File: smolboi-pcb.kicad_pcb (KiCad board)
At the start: 2 copper layers, 228.6 x 88.9 mm, 114 parts, among them SW1 ESC, SW10 O, SW11 P, SW12 Bksp, SW13 Tab, SW14 A, SW15 S, SW16 D, SW17 F, SW18 G, SW19 H, SW2 Q, SW20 J, SW21 K, SW22 L, SW23 ;, SW24 ', SW25 Shift, SW26 Z, SW27 X, SW28 C, SW29 V, SW3 W, SW30 B, SW31 N, SW32 M, SW33 ,, SW34 ., SW35 /, SW36 CpsLk, SW37 Ctrl, SW38 Win, SW39 Alt, SW4 E, SW40 FUP, SW41 FDN, SW42 Space, SW43 FRI, SW44 Left, SW45 Del, SW46 Enter, SW47 SW_Push, SW48 SW_Push, SW5 R, SW6 T, SW7 Y, SW8 U, SW9 I, U1 STM32F103C8Tx, U2 PRTR5V0U2X, U3 XC6206, Y1 8MHz

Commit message: staggered layout, routed diff pair on right side
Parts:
- SW1, SW10, SW11, SW14, SW15, SW16, SW17, SW18, SW19, SW2, SW20, SW21, SW22, SW23, SW26, SW27, SW28, SW29, SW3, SW30, SW31, SW32, SW33, SW34, SW35, SW36, SW4, SW40, SW41, SW43, SW44, SW45, SW46, SW5, SW6, SW7, SW8, SW9: footprint MX_Only:MXOnly-1U-Hotswap -> MX_Only:MXOnly-1U-NoLED
- SW12, SW25: footprint MX_Only:MXOnly-1U-Hotswap -> MX_Only:MXOnly-1.75U-NoLED
- SW13, SW37, SW38, SW39: footprint MX_Only:MXOnly-1U-Hotswap -> MX_Only:MXOnly-1.25U-NoLED
- SW24: footprint MX_Only:MXOnly-1U-Hotswap -> MX_Only:MXOnly-1.5U-NoLED
- SW42: footprint MX_Only:MXOnly-3U-Hotswap -> MX_Only:MXOnly-2U-NoLED
- moved SW48 80.4 mm to (350.3, 119.0), turned to 0 degrees
- moved C8 77.0 mm to (356.6, 57.1)
- moved C9 77.0 mm to (352.7, 55.4)
- moved U3 77.0 mm to (355.1, 55.4)
- moved R3 76.2 mm to (351.0, 45.5)
- moved U2 76.2 mm to (349.2, 50.8)
- moved USB1 76.2 mm to (349.2, 34.5)
- moved R4 76.0 mm to (347.5, 45.5)
- moved F1 74.4 mm to (342.6, 55.9)
- moved R5 72.2 mm to (345.3, 119.0), turned to 90 degrees
- moved C5 67.3 mm to (339.2, 109.1)
- moved U1 67.3 mm to (334.8, 104.6)
- moved C2 67.3 mm to (338.8, 99.6)
- moved C3 67.3 mm to (329.9, 100.7)
- moved C4 67.3 mm to (333.7, 111.0)
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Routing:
- net col2: track 60.9 -> 0.00 mm
- net col6: track 60.9 -> 0.00 mm
- net col1: track 60.8 -> 0.00 mm
- net col0: track 60.8 -> 0.00 mm
- net col10: track 60.7 -> 0.00 mm
- net col4: track 60.6 -> 0.00 mm
- net col11: track 60.4 -> 0.00 mm
- net col3: track 60.4 -> 0.00 mm
- net col8: track 60.3 -> 0.00 mm
- net col9: track 59.7 -> 0.00 mm
- net col5: track 44.1 -> 0.00 mm
- net col7: track 40.2 -> 0.00 mm
- net BOOT0: track 0.00 -> 9.03 mm
- net Net-(R4-Pad1): track 0.00 -> 2.96 mm
- net Net-(R3-Pad1): track 0.00 -> 2.72 mm
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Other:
- board size 228.6 x 88.9 mm -> 242.9 x 87.6 mm

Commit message: gnd fill around oscillator, all pwr routed, NRST vias
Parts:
- moved C9 18.7 mm to (335.0, 61.5), turned to 180 degrees
- moved U3 17.9 mm to (338.2, 61.4)
- moved C8 15.6 mm to (341.6, 61.4)
- moved D42 13.5 mm to (283.8, 110.5), turned to 90 degrees
- moved D44 8.90 mm to (359.4, 111.1), turned to 180 degrees
- moved D10 6.29 mm to (336.6, 53.3)
- moved D12 5.82 mm to (382.3, 53.3)
- moved D15 5.68 mm to (208.3, 72.4)
- moved D16 5.68 mm to (227.3, 72.4)
- moved D41 5.68 mm to (255.9, 110.5)
- moved D14 5.68 mm to (189.2, 72.4)
- moved D17 5.68 mm to (246.4, 72.4)
- moved D20 5.68 mm to (303.5, 72.4)
- moved D21 5.68 mm to (322.6, 72.4)
- moved D22 5.68 mm to (341.6, 72.4)
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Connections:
- SW43 pad 2: col8 -> col7
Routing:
- net row2: track 0.00 -> 209.1 mm
- net row1: track 0.00 -> 205.4 mm
- net row0: track 0.00 -> 202.1 mm
- net row3: track 0.00 -> 176.6 mm
- net +3V3: track 0.00 -> 129.2 mm, vias 0 -> 7
- net GND: track 0.00 -> 119.1 mm, vias 0 -> 5
- net col6: track 0.00 -> 67.3 mm
- net col1: track 0.00 -> 66.3 mm
- net col9: track 0.00 -> 65.9 mm
- net col2: track 0.00 -> 64.3 mm
- net col10: track 0.00 -> 63.3 mm
- net col4: track 0.00 -> 63.3 mm
- net col3: track 0.00 -> 63.3 mm
- net col7: track 0.00 -> 63.3 mm
- net col0: track 0.00 -> 62.5 mm
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- added copper zone on B.Cu, net GND
- added copper zone on F.Cu, net GND
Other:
- outline, holes or cut-outs redrawn
- net class Power: trace_width 0.381 -> 0.3

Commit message: routed matrix
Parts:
- removed SW47: SW_Push, Button_Switch_SMD:SW_SPST_SKQG_WithStem
- moved C1 8.29 mm to (330.2, 112.6), turned to 180 degrees
- moved R5 6.05 mm to (342.7, 113.5)
- moved SW48 6.05 mm to (347.7, 113.5)
- moved C4 1.01 mm to (330.2, 111.4)
- moved C9 0.30 mm to (335.3, 61.4), turned to 270 degrees
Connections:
- U1 pad 14: Net-(U1-Pad14) -> col0
- U1 pad 15: Net-(U1-Pad15) -> col1
- U1 pad 16: Net-(U1-Pad16) -> col2
- U1 pad 17: Net-(U1-Pad17) -> col3
- U1 pad 18: Net-(U1-Pad18) -> col4
- U1 pad 19: Net-(U1-Pad19) -> col5
- U1 pad 20: Net-(U1-Pad20) -> col6
- U1 pad 21: Net-(U1-Pad21) -> col7
- U1 pad 22: Net-(U1-Pad22) -> col8
- U1 pad 37: Net-(U1-Pad37) -> row2
- U1 pad 38: Net-(U1-Pad38) -> row0
- U1 pad 39: Net-(U1-Pad39) -> row1
- U1 pad 40: Net-(U1-Pad40) -> col11
- U1 pad 41: Net-(U1-Pad41) -> col10
- U1 pad 42: Net-(U1-Pad42) -> col9
- U1 pad 43: Net-(U1-Pad43) -> row3
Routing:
- net col0: track 62.5 -> 225.5 mm
- net col1: track 66.3 -> 205.1 mm
- net col2: track 64.3 -> 175.2 mm, vias 0 -> 1
- net row0: track 202.1 -> 311.4 mm, vias 0 -> 4
- net col3: track 63.3 -> 155.3 mm, vias 0 -> 1
- net col4: track 63.3 -> 136.3 mm, vias 0 -> 1
- net row3: track 176.6 -> 249.5 mm, vias 0 -> 2
- net row1: track 205.4 -> 271.5 mm, vias 0 -> 4
- net col5: track 44.0 -> 104.1 mm, vias 0 -> 1
- net col11: track 60.4 -> 118.9 mm
- net col10: track 63.3 -> 102.6 mm
- net col6: track 67.3 -> 104.7 mm, vias 0 -> 1
- net GND: track 119.1 -> 155.2 mm, vias 5 -> 9
- net row2: track 209.1 -> 242.4 mm, vias 0 -> 2
- net col8: track 44.0 -> 74.5 mm, vias 0 -> 1
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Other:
- board size 242.9 x 87.6 mm -> 242.9 x 83.9 mm

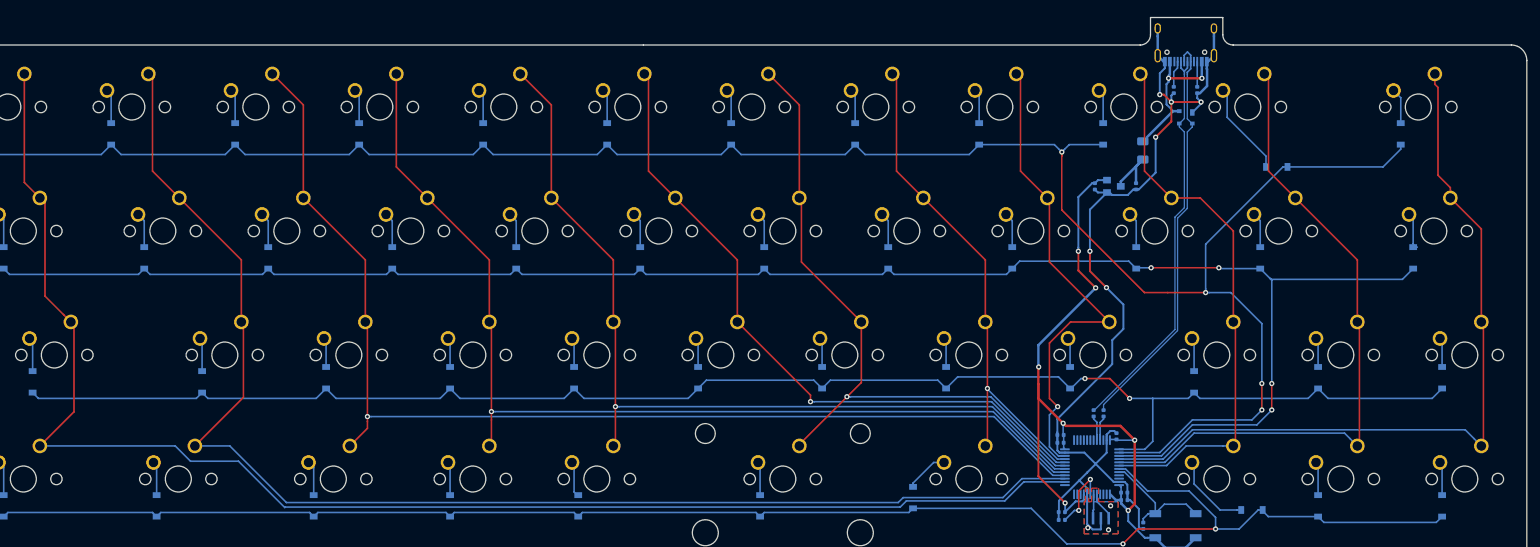
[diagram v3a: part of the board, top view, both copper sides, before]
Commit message: inc USB C solder pad margin
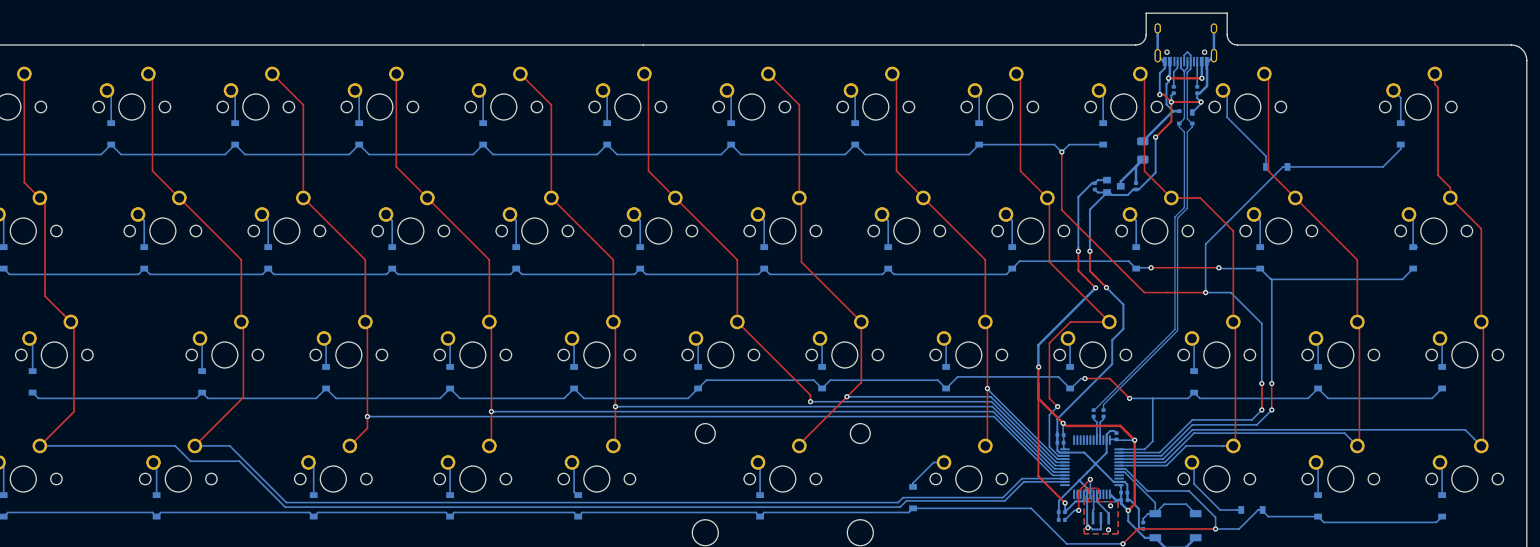
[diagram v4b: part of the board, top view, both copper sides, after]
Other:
- board size 242.9 x 83.9 mm -> 242.9 x 84.6 mm
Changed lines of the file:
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@@
     (thickness 1.6)
     (drawings 15)
-    (tracks 733)
+    (tracks 732)
     (zones 0)
     (modules 113)
@@
     (38 B.Mask user)
     (39 F.Mask user)
-    (40 Dwgs.User user hide)
+    (40 Dwgs.User user)
     (41 Cmts.User user)
     (42 Eco1.User user)
@@
     )
   )
-  (gr_line (start 342.23325 39.6875) (end 265.90625 39.6875) (layer Edge.Cuts) (width 0.05))
-  (gr_line (start 399.25625 39.6875) (end 356.52075 39.6875) (layer Edge.Cuts) (width 0.05))
+  (gr_line (start 341.5665 39.6875) (end 265.90625 39.6875) (layer Edge.Cuts) (width 0.05))
+  (gr_line (start 399.25625 39.6875) (end 357.1875 39.6875) (layer Edge.Cuts) (width 0.05))
   (gr_line (start 399.25625 119.38) (end 161.13125 119.38) (layer Edge.Cuts) (width 0.05))
   (gr_arc (start 399.25625 116.99875) (end 399.25625 119.38) (angle -90) (layer Edge.Cuts) (width 0.05))
@@
   (gr_line (start 161.13125 39.6875) (end 265.90625 39.6875) (layer Edge.Cuts) (width 0.05))
   (gr_arc (start 161.13125 42.06875) (end 161.13125 39.6875) (angle -90) (layer Edge.Cuts) (width 0.05))
-  (gr_line (start 354.93325 35.46475) (end 354.93325 38.1) (layer Edge.Cuts) (width 0.05))
-  (gr_line (start 343.82075 35.46475) (end 354.93325 35.46475) (layer Edge.Cuts) (width 0.05))
-  (gr_line (start 343.82075 38.1) (end 343.82075 35.46475) (layer Edge.Cuts) (width 0.05))
-  (gr_arc (start 356.52075 38.1) (end 354.93325 38.1) (angle -90) (layer Edge.Cuts) (width 0.05))
-  (gr_arc (start 342.23325 38.1) (end 342.23325 39.6875) (angle -90) (layer Edge.Cuts) (width 0.05))
+  (gr_line (start 355.6 34.798) (end 355.6 38.1) (layer Edge.Cuts) (width 0.05))
+  (gr_line (start 343.154 34.798) (end 355.6 34.798) (layer Edge.Cuts) (width 0.05))
+  (gr_line (start 343.154 38.1) (end 343.154 34.798) (layer Edge.Cuts) (width 0.05))
+  (gr_arc (start 357.1875 38.1) (end 355.6 38.1) (angle -90) (layer Edge.Cuts) (width 0.05))
+  (gr_arc (start 341.5665 38.1) (end 341.5665 39.6875) (angle -90) (layer Edge.Cuts) (width 0.05))
   (segment (start 352.655 42.239) (end 353.57 41.324) (width 0.381) (layer B.Cu) (net 1))
   (segment (start 352.475 42.239) (end 352.655 42.239) (width 0.381) (layer B.Cu) (net 1))
@@
   (segment (start 177.95875 82.2325) (end 178.435 82.70875) (width 0.25) (layer F.Cu) (net 61))
   (segment (start 178.435 82.70875) (end 178.435 96.04375) (width 0.25) (layer F.Cu) (net 61))
-  (segment (start 193.9925 101.2825) (end 173.19625 101.2825) (width 0.25) (layer B.Cu) (net 61))
-  (segment (start 196.342 103.632) (end 193.9925 101.2825) (width 0.25) (layer B.Cu) (net 61))
-  (segment (start 210.82 110.744) (end 203.708 103.632) (width 0.25) (layer B.Cu) (net 61))
-  (segment (start 203.708 103.632) (end 196.342 103.632) (width 0.25) (layer B.Cu) (net 61))
-  (segment (start 324.36366 106.80275) (end 321.43841 109.728) (width 0.25) (layer B.Cu) (net 61))
-  (segment (start 330.673 106.80275) (end 324.36366 106.80275) (width 0.25) (layer B.Cu) (net 61))
-  (segment (start 321.43841 109.728) (end 306.324 109.728) (width 0.25) (layer B.Cu) (net 61))
-  (segment (start 306.324 109.728) (end 305.377009 110.674991) (width 0.25) (layer B.Cu) (net 61))
-  (segment (start 305.377009 110.674991) (end 210.889009 110.674991) (width 0.25) (layer B.Cu) (net 61))
-  (segment (start 210.889009 110.674991) (end 210.82 110.744) (width 0.25) (layer B.Cu) (net 61))
+  (segment (start 324.36366 106.80275) (end 330.673 106.80275) (width 0.25) (layer B.Cu) (net 61))
+  (segment (start 321.43841 109.728) (end 324.36366 106.80275) (width 0.25) (layer B.Cu) (net 61))
+  (segment (start 306.324 109.728) (end 321.43841 109.728) (width 0.25) (layer B.Cu) (net 61))
+  (segment (start 193.9925 101.2825) (end 196.342 103.632) (width 0.25) (layer B.Cu) (net 61))
+  (segment (start 173.19625 101.2825) (end 193.9925 101.2825) (width 0.25) (layer B.Cu) (net 61))
+  (segment (start 196.342 103.632) (end 203.846018 103.632) (width 0.25) (layer B.Cu) (net 61))
+  (segment (start 203.846018 103.632) (end 210.889009 110.674991) (width 0.25) (layer B.Cu) (net 61))
+  (segment (start 210.889009 110.674991) (end 305.377009 110.674991) (width 0.25) (layer B.Cu) (net 61))
+  (segment (start 305.377009 110.674991) (end 306.324 109.728) (width 0.25) (layer B.Cu) (net 61))
   (segment (start 190.5 59.055) (end 194.6275 63.1825) (width 0.25) (layer F.Cu) (net 62))
   (segment (start 189.865 44.1325) (end 190.5 44.7675) (width 0.25) (layer F.Cu) (net 62))

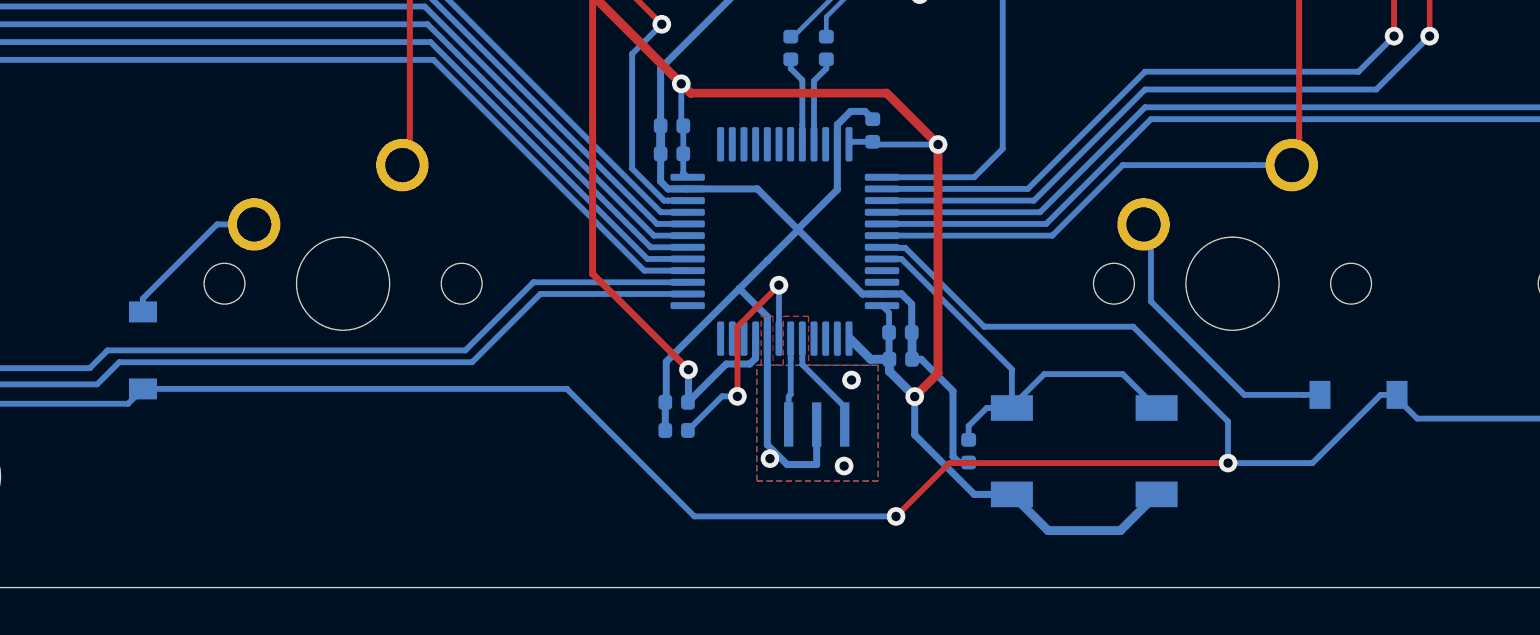
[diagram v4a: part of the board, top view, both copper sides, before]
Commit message: replaced with STM32F072CBT6, rerouted
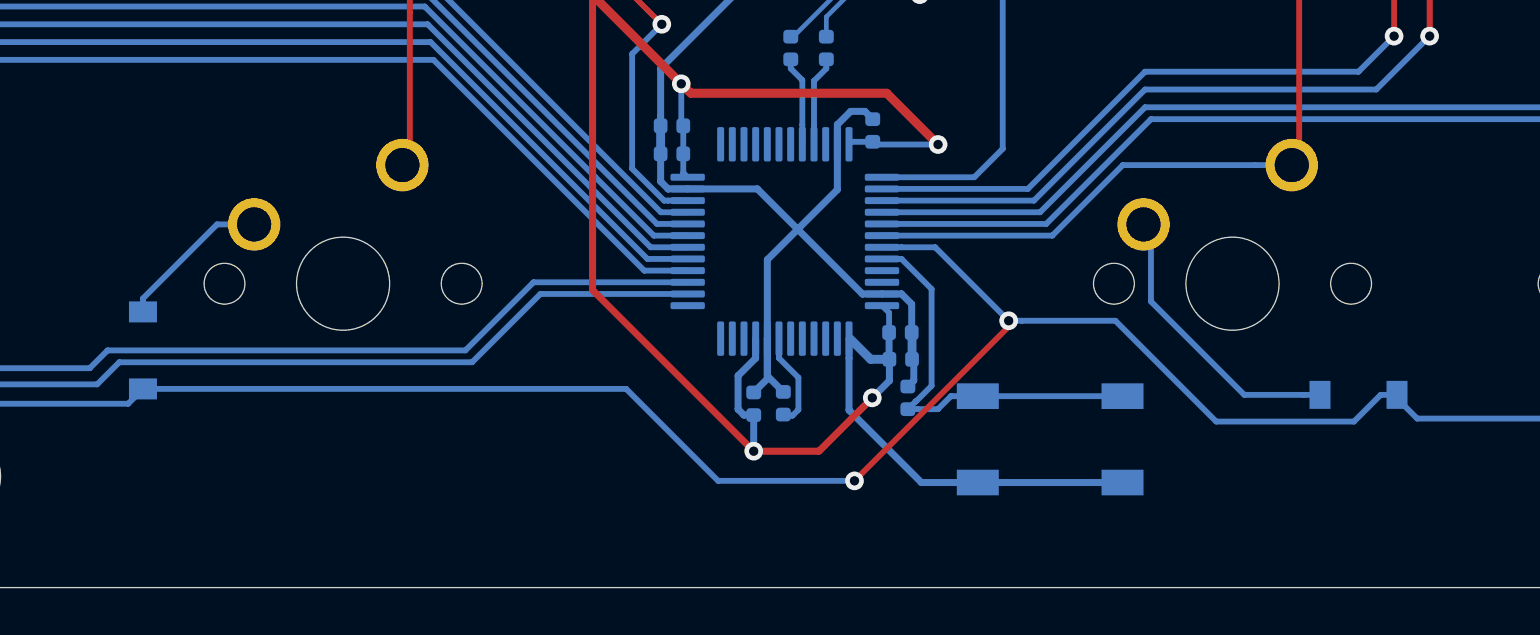
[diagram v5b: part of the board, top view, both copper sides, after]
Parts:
- removed SW48: SW_Push, Button_Switch_SMD:SW_SPST_SKQG_WithStem
- removed Y1: 8MHz, CSTNE8M00GH5C000R0:OSC_CSTNE8M00GH5C000R0
- added SW47: SW_Push, Button_Switch_SMD:SW_SPST_SKQG_WithStem, B.Cu at (346.2, 113.0)
- U1: value STM32F103C8Tx -> STM32F072CBTx
- moved C1 4.72 mm to (334.8, 111.5), turned to 90 degrees
- moved R5 3.46 mm to (340.1, 111.3), turned to 270 degrees
- moved C4 3.30 mm to (333.5, 111.5), turned to 90 degrees
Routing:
- net GND: track 155.2 -> 138.6 mm, vias 9 -> 6
- net row3: track 249.5 -> 239.0 mm
- net Net-(C1-Pad1): track 10.5 -> 4.16 mm, vias 2 -> 0
- net Net-(U1-Pad5): track 4.43 -> 0.00 mm
- net Net-(U1-Pad6): track 3.72 -> 0.00 mm
- net BOOT0: track 19.4 -> 17.7 mm
- net +3V3: track 125.3 -> 126.1 mm
- removed copper zone on B.Cu, net GND
- removed copper zone on F.Cu, net GND

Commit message: ground fills
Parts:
- moved SW47 1.52 mm to (347.7, 113.0)
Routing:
- net BOOT0: track 17.7 -> 19.2 mm
- net +3V3: track 126.1 -> 127.6 mm
- net row3: track 239.0 -> 239.5 mm
- added copper zone on B.Cu, net GND
- added copper zone on F.Cu, net GND
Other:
- board text added: "smolboi V1.0 August 2024"
